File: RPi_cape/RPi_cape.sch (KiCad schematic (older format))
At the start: 109 parts, among them J1 Conn_01x04, J10 Conn_01x02, J11 Conn_01x02, J12 Conn_01x02, J16 Conn_01x06, J2 Conn_01x02, J3 Conn_01x02, J4 Conn_01x02, J5 Conn_01x03, J6 Conn_01x03, J7 Conn_01x02, J8 Conn_02x20_Odd_Even, J9 Conn_01x02, U1 TL431A, U2 ADC128D818, U3 ADC128D818

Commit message: Better valve monitoring, finalized layout and manufacturing files
Created assembly and fabrication drawings, assigned all BOM parts, generally made design ready for ordering
Added strain-relief slots and barb mounting dimensions for digital pressure sensors
Changed valve drivers from discrete power MOSFETs to "smart" industrial/automotive driver ICs for the current monitoring, including valve-movement monitor for #4
Connected RPi_Valve* signals to larger CPLD footprint, changed Raspberry Pi pin assignment as a result to ease PCB routing
Updated footprints, page layout to create readable assembly drawing
Added current-measurement testpoints for CPLD power from BATT+
Changed power diodes in power-down-alarm circuit to small-signal parts for more compact layout
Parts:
- removed C15, C16, C17, C18: 100uF 50V AlPoly, Capacitor_SMD:CP_Elec_10x10.5, symbol Device:CP1
- removed H5: #4/M3, MountingHole:MountingHole_3.2mm_M3_Pad_Via, symbol Mechanical:MountingHole_Pad
- added C29, C30, C49: 10nF 50V NP0, Capacitor_SMD:C_0603_1608Metric, symbol Device:C
- D1, D2: footprint Diode_SMD:D_SMA -> Ventilator:D_SMA
- D3: footprint Diode_SMD:D_SOD-123 -> Ventilator:D_SOD-123; Manufacturer (none) -> ON Semiconductor; Part Number (none) -> MMSZ5231BT1G
- D4, D5, D6, D7, D8, D9: footprint LED_SMD:LED_0805_2012Metric -> Ventilator:LED_0805_2012Metric
- R1, R2: Manufacturer (none) -> KOA Speer; Part Number (none) -> RK73H2BTTD1001F
- R10, R16, R18: Manufacturer (none) -> KOA Speer; Part Number (none) -> RK73H2BTTD10R0F
- R11, R4: Manufacturer (none) -> Panasonic; Part Number (none) -> ERJ-8GEY0R00V
- R12, R13, R19, R192, R195, R196, R197, R25, R26, R27, R28, R6, R7: Manufacturer (none) -> KOA Speer; Part Number (none) -> RK73H2BTTD1002F
- R14, R15, R17, R193, R194: Manufacturer (none) -> KOA Speer; Part Number (none) -> RK73H2BTTD3301F
- R20, R22: Manufacturer (none) -> KOA Speer; Part Number (none) -> RK73H2BTTD2202F
- R29: Manufacturer (none) -> KOA Speer; Part Number (none) -> RK73H2BTTD1501F
- R5: Manufacturer (none) -> Panasonic; Part Number (none) -> ERJ-8RQF1R0V
- R8: value 10K -> DNP
- R9: value 1K -> DNP
- U1: footprint Package_TO_SOT_SMD:SOT-23 -> Ventilator:SOT-23
- U2, U3: footprint Package_SO:TSSOP-16_4.4x5mm_P0.65mm -> Ventilator:TSSOP-16_4.4x5mm_P0.65mm
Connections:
- net CPLD_ADC3: now also C29.2
- net CPLD_ADC4: now also C30.2
- net CPLD_ADC5: now also C49.2
- net CPLD_ADC6: now also C5.2, R8.2, R9.1; no longer C4.2, R6.2, R7.1
- net CPLD_ADC7: now also C4.2, R6.2, R7.1; no longer C5.2, R8.2, R9.1
- net GND: now also C29.1, C30.1, C49.1
- net Output Driver 1/OutH: now also J9.2 (Pin_2); no longer J9.1 (Pin_1)
- net Output Driver 1/OutL: now also J9.1 (Pin_1); no longer J9.2 (Pin_2)
- net Output Driver 2/OutH: now also J10.2 (Pin_2); no longer J10.1 (Pin_1)
- net Output Driver 2/OutL: now also J10.1 (Pin_1); no longer J10.2 (Pin_2)
- net Output Driver 3/OutH: now also J11.2 (Pin_2); no longer J11.1 (Pin_1)
- net Output Driver 3/OutL: now also J11.1 (Pin_1); no longer J11.2 (Pin_2)
- net Output Driver 4/OutH: now also J12.2 (Pin_2); no longer J12.1 (Pin_1)
- net Output Driver 4/OutL: now also J12.1 (Pin_1); no longer J12.2 (Pin_2)
- net RPi_Alarm_Spkr: now also J8.11 (Pin_11); no longer J8.21 (Pin_21)
- net RPi_valve1: now also J8.40 (Pin_40); no longer J8.11 (Pin_11)
- net RPi_valve2: now also J8.38 (Pin_38); no longer J8.13 (Pin_13)
- net RPi_valve3: now also J8.36 (Pin_36); no longer J8.15 (Pin_15)
- net RPi_valve4: now also J8.32 (Pin_32); no longer J8.19 (Pin_19)
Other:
- note added: "Alarm(s)"
- note added: "Populate (10K, 1K) if not using\nthe valve driver current sense"
- note added: "When analog current sense drivers used,\nCPLD fault input for valve 4 is handled by\n"valve motion detection" circuit\n(all other valve fault inputs are inactive)"
- moved on the sheet: F4, F5, J10, J11, J12, J5, J6, J7, J9

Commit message: Manufacturing clean-up
Corrections and additions to BOM etc. for manufacturing
Added power draw tracking spreadsheet
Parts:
- C113, C40, C43: Manufacturer Murata -> AVX; Part Number GRM1885C1H103JA01D -> 06035A102JAT2A
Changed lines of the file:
@@
 F 2 "Capacitor_SMD:C_0603_1608Metric" H 11338 9700 50  0001 C CNN
 F 3 "~" H 11300 9850 50  0001 C CNN
-F 4 "Murata" H 11300 9850 50  0001 C CNN "Manufacturer"
-F 5 "GRM1885C1H103JA01D" H 11300 9850 50  0001 C CNN "Part Number"
+F 4 "AVX" H 11300 9850 50  0001 C CNN "Manufacturer"
+F 5 "06035A102JAT2A" H 11300 9850 50  0001 C CNN "Part Number"
 	1    11300 9850
 	-1   0    0    1
@@
 F 2 "Capacitor_SMD:C_0603_1608Metric" H 11588 9700 50  0001 C CNN
 F 3 "~" H 11550 9850 50  0001 C CNN
-F 4 "Murata" H 11550 9850 50  0001 C CNN "Manufacturer"
-F 5 "GRM1885C1H103JA01D" H 11550 9850 50  0001 C CNN "Part Number"
+F 4 "AVX" H 11550 9850 50  0001 C CNN "Manufacturer"
+F 5 "06035A102JAT2A" H 11550 9850 50  0001 C CNN "Part Number"
 	1    11550 9850
 	-1   0    0    1
@@
 F 2 "Capacitor_SMD:C_0603_1608Metric" H 10488 10000 50  0001 C CNN
 F 3 "~" H 10450 10150 50  0001 C CNN
-F 4 "Murata" H 10450 10150 50  0001 C CNN "Manufacturer"
-F 5 "GRM1885C1H103JA01D" H 10450 10150 50  0001 C CNN "Part Number"
+F 4 "AVX" H 10450 10150 50  0001 C CNN "Manufacturer"
+F 5 "06035A102JAT2A" H 10450 10150 50  0001 C CNN "Part Number"
 	1    10450 10150
 	-1   0    0    1

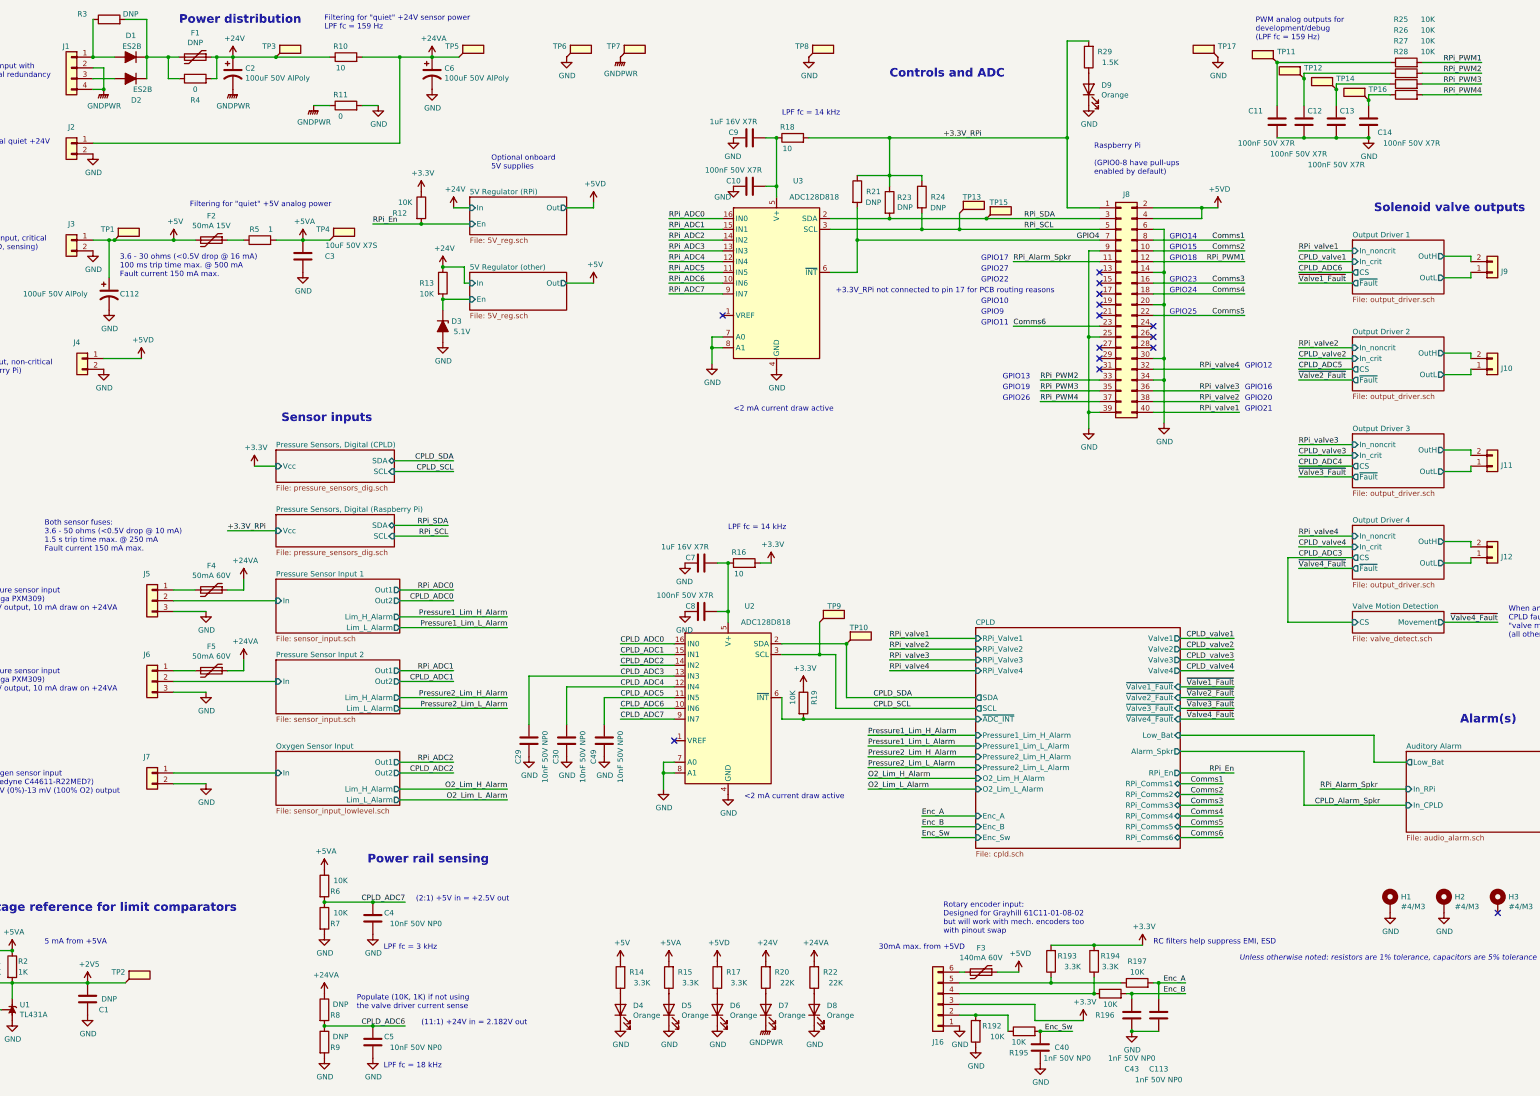
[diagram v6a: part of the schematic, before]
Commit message: Safety additions
Switched CPLD_ADC7 to +24V monitoring (from +5V monitoring), and added CPLD ~Bat_On digital input(s) to know when it's running from backup battery, to cover low-input-voltage edge cases
Added series 1K resistors (R226-231) on CPLD<->RPi Comms1-6 lines, to protect CPLD in case of overvoltage from RPi failure
Added optional input TVS D23 to handle sustained over-voltage or large surges
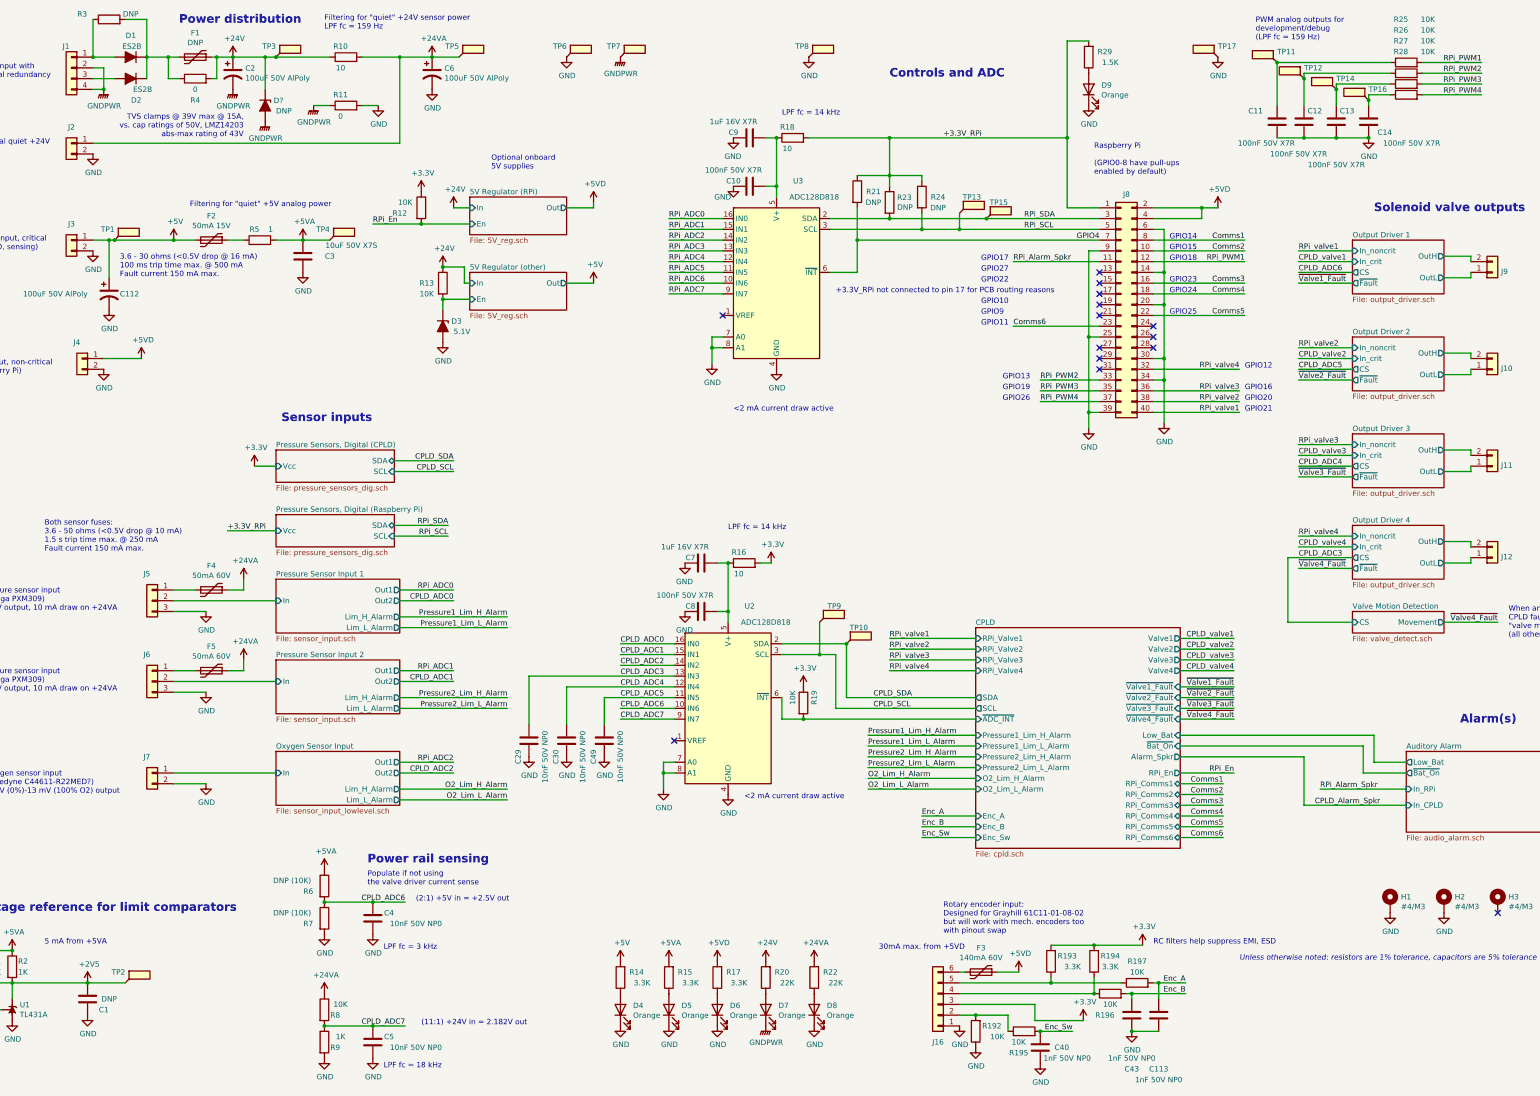
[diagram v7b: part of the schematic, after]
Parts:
- added D?: DNP, Ventilator:D_SMB, symbol Device:D_Zener_ALT
- R6, R7: value 10K -> DNP (10K)
- R8: value DNP -> 10K; Manufacturer (none) -> KOA Speer; Part Number (none) -> RK73H2BTTD1002F
- R9: value DNP -> 1K; Manufacturer (none) -> KOA Speer; Part Number (none) -> RK73H2BTTD1001F
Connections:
- net +24V: now also D?.1 (K)
- net CPLD_ADC6: now also C4.2, R6.2, R7.1; no longer C5.2, R8.2, R9.1
- net CPLD_ADC7: now also C5.2, R8.2, R9.1; no longer C4.2, R6.2, R7.1
- net GNDPWR: now also D?.2 (A)
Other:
- note added: "Populate if not using\nthe valve driver current sense"
- note added: "TVS clamps @ 39V max @ 15A,\nvs. cap ratings of 50V, LMZ14203\nabs-max rating of 43V"
- note removed: "Populate (10K, 1K) if not using\nthe valve driver current sense"
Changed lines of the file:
@@
 Title "Raspberry Pi Hat for JamVent Adaptation"
 Date ""
-Rev "1.5"
+Rev "1.6"
 Comp "Partners COVID Innovation Group"
 Comment1 "Don Straney"
@@
 F3 "In_CPLD" I L 13850 7900 50
 F4 "Low_Bat" O L 13850 7500 50
+F5 "~Bat_On" O L 13850 7600 50
 $EndSheet
 $Comp
@@
 $EndComp
 Wire Wire Line
-	2950 950  3350 950
+	2950 950  3250 950
 $Comp
 L Ventilator:+24VA #PWR029
@@
 AR Path="/5E9D7F90" Ref="R6"  Part="1"
 AR Path="/5E8AFE9D/5E9D7F90" Ref="R?"  Part="1"
-F 0 "R6" H 3900 8600 50  0000 C CNN
-F 1 "10K" H 3950 8700 50  0000 C CNN
+F 0 "R6" H 3650 8600 50  0000 C CNN
+F 1 "DNP (10K)" H 3500 8700 50  0000 C CNN
 F 2 "Resistor_SMD:R_1206_3216Metric" V 3730 8650 50  0001 C CNN
 F 3 "~" H 3800 8650 50  0001 C CNN
@@
 AR Path="/5E9DF1E8" Ref="R7"  Part="1"
 AR Path="/5E8AFE9D/5E9DF1E8" Ref="R?"  Part="1"
-F 0 "R7" H 3900 8900 50  0000 C CNN
-F 1 "10K" H 3950 9000 50  0000 C CNN
+F 0 "R7" H 3650 8900 50  0000 C CNN
+F 1 "DNP (10K)" H 3500 9000 50  0000 C CNN
 F 2 "Resistor_SMD:R_1206_3216Metric" V 3730 8950 50  0001 C CNN
 F 3 "~" H 3800 8950 50  0001 C CNN
@@
 AR Path="/5E8AFE9D/5E9DF420" Ref="R?"  Part="1"
 F 0 "R8" H 3900 9750 50  0000 C CNN
-F 1 "DNP" H 3950 9850 50  0000 C CNN
+F 1 "10K" H 3950 9850 50  0000 C CNN
 F 2 "Resistor_SMD:R_1206_3216Metric" V 3730 9800 50  0001 C CNN
 F 3 "~" H 3800 9800 50  0001 C CNN
+F 4 "KOA Speer" H 3800 9800 50  0001 C CNN "Manufacturer"
+F 5 "RK73H2BTTD1002F" H 3800 9800 50  0001 C CNN "Part Number"
 	1    3800 9800
 	1    0    0    -1
@@
 AR Path="/5E8AFE9D/5E9DF8CA" Ref="R?"  Part="1"
 F 0 "R9" H 3900 10050 50  0000 C CNN
-F 1 "DNP" H 3950 10150 50  0000 C CNN
+F 1 "1K" H 3950 10150 50  0000 C CNN
 F 2 "Resistor_SMD:R_1206_3216Metric" V 3730 10100 50  0001 C CNN
 F 3 "~" H 3800 10100 50  0001 C CNN
+F 4 "KOA Speer" H 3800 10100 50  0001 C CNN "Manufacturer"
+F 5 "RK73H2BTTD1001F" H 3800 10100 50  0001 C CNN "Part Number"
 	1    3800 10100
 	1    0    0    -1
@@
 Wire Wire Line
 	4500 7850 5500 7850
-$Sheet
-S 9850 6250 1900 2050
-U 5E8C8865
-F0 "CPLD" 50
-F1 "cpld.sch" 50
-F2 "Valve1" O R 11750 6350 50
-F3 "Valve2" O R 11750 6450 50
-F4 "Valve3" O R 11750 6550 50
-F5 "Valve4" O R 11750 6650 50
-F6 "RPi_Valve1" I L 9850 6350 50
-F7 "RPi_Valve2" I L 9850 6450 50
-F8 "RPi_Valve3" I L 9850 6550 50
-F9 "RPi_Valve4" I L 9850 6650 50
-F10 "Pressure1_Lim_H_Alarm" I L 9850 7250 50
-F11 "Pressure1_Lim_L_Alarm" I L 9850 7350 50
-F12 "Pressure2_Lim_H_Alarm" I L 9850 7450 50
-F13 "Pressure2_Lim_L_Alarm" I L 9850 7550 50
-F14 "O2_Lim_H_Alarm" I L 9850 7650 50
-F15 "O2_Lim_L_Alarm" I L 9850 7750 50
-F16 "Alarm_Spkr" O R 11750 7400 50
-F17 "SDA" O L 9850 6900 50
-F18 "SCL" O L 9850 7000 50
-F19 "~ADC_INT" I L 9850 7100 50
-F20 "Low_Bat" I R 11750 7250 50
-F21 "RPi_Comms1" B R 11750 7700 50
-F22 "RPi_Comms2" B R 11750 7800 50
-F23 "RPi_Comms3" B R 11750 7900 50
-F24 "RPi_Comms4" B R 11750 8000 50
-F25 "RPi_Comms5" B R 11750 8100 50
-F26 "RPi_Comms6" B R 11750 8200 50
-F27 "RPi_En" O R 11750 7600 50
-F28 "Enc_A" I L 9850 8000 50
-F29 "Enc_B" I L 9850 8100 50
-F30 "Enc_Sw" I L 9850 8200 50
-F31 "~Valve1_Fault" I R 11750 6800 50
-F32 "~Valve2_Fault" I R 11750 6900 50
-F33 "~Valve4_Fault" I R 11750 7100 50
-F34 "~Valve3_Fault" I R 11750 7000 50
-$EndSheet
 Wire Wire Line
 	9850 6350 9050 6350
@@
 Text Label 6550 7100 0    50   ~ 0
 CPLD_ADC7
-Text Label 4550 9950 2    50   ~ 0
-CPLD_ADC6
 Text Label 4550 8800 2    50   ~ 0
+CPLD_ADC6
+Text Label 4550 9950 2    50   ~ 0
 CPLD_ADC7
 Wire Wire Line
@@
 GPIO9
 Wire Wire Line
-	12900 7400 12900 7900
+	12900 7450 12900 7900
 Wire Wire Line
 	12900 7900 13850 7900
@@
 	11750 7250 13550 7250
 Wire Wire Line
-	11750 7400 12900 7400
+	11750 7450 12900 7450
 Wire Wire Line
 	11750 7700 12150 7700
@@
 Text Label 12850 2950 0    50   ~ 0
 CPLD_ADC6
-Text Notes 4100 9800 0    50   ~ 0
-Populate (10K, 1K) if not using\nthe valve driver current sense
+Text Notes 4200 8650 0    50   ~ 0
+Populate if not using\nthe valve driver current sense
 $Comp
 L Connector_Generic:Conn_02x20_Odd_Even J8
@@
 Text Notes 14350 7150 0    79   ~ 16
 Alarm(s)
+Wire Wire Line
+	13850 7600 13450 7600
+Wire Wire Line
+	13450 7600 13450 7350
+Wire Wire Line
+	13450 7350 11750 7350
+$Sheet
+S 9850 6250 1900 2050
+U 5E8C8865
+F0 "CPLD" 50
+F1 "cpld.sch" 50
+F2 "Valve1" O R 11750 6350 50
+F3 "Valve2" O R 11750 6450 50
+F4 "Valve3" O R 11750 6550 50
+F5 "Valve4" O R 11750 6650 50
+F6 "RPi_Valve1" I L 9850 6350 50
+F7 "RPi_Valve2" I L 9850 6450 50
+F8 "RPi_Valve3" I L 9850 6550 50
+F9 "RPi_Valve4" I L 9850 6650 50
+F10 "Pressure1_Lim_H_Alarm" I L 9850 7250 50
+F11 "Pressure1_Lim_L_Alarm" I L 9850 7350 50
+F12 "Pressure2_Lim_H_Alarm" I L 9850 7450 50
+F13 "Pressure2_Lim_L_Alarm" I L 9850 7550 50
+F14 "O2_Lim_H_Alarm" I L 9850 7650 50
+F15 "O2_Lim_L_Alarm" I L 9850 7750 50
+F16 "Alarm_Spkr" O R 11750 7450 50
+F17 "SDA" O L 9850 6900 50
+F18 "SCL" O L 9850 7000 50
+F19 "~ADC_INT" I L 9850 7100 50
+F20 "Low_Bat" I R 11750 7250 50
+F21 "RPi_Comms1" B R 11750 7700 50
+F22 "RPi_Comms2" B R 11750 7800 50
+F23 "RPi_Comms3" B R 11750 7900 50
+F24 "RPi_Comms4" B R 11750 8000 50
+F25 "RPi_Comms5" B R 11750 8100 50
+F26 "RPi_Comms6" B R 11750 8200 50
+F27 "RPi_En" O R 11750 7600 50
+F28 "Enc_A" I L 9850 8000 50
+F29 "Enc_B" I L 9850 8100 50
+F30 "Enc_Sw" I L 9850 8200 50
+F31 "~Valve1_Fault" I R 11750 6800 50
+F32 "~Valve2_Fault" I R 11750 6900 50
+F33 "~Valve4_Fault" I R 11750 7100 50
+F34 "~Valve3_Fault" I R 11750 7000 50
+F35 "~Bat_On" I R 11750 7350 50
+$EndSheet
+$Comp
+L Device:D_Zener_ALT D?
+U 1 1 5F21EF66
+P 3250 1400
+AR Path="/5F21EF66" Ref="D?"  Part="1"
+AR Path="/5E8AFE9D/5F21EF66" Ref="D?"  Part="1"
+AR Path="/5E8FBD97/5F21EF66" Ref="D?"  Part="1"
+AR Path="/5E8DEDC0/5F21EF66" Ref="D?"  Part="1"
+AR Path="/5E8DFCAD/5F21EF66" Ref="D?"  Part="1"
+AR Path="/5E8E0754/5F21EF66" Ref="D?"  Part="1"
+F 0 "D?" V 3204 1479 50  0000 L CNN
+F 1 "DNP" V 3300 1500 50  0000 L CNN
+F 2 "Ventilator:D_SMB" H 3250 1400 50  0001 C CNN
+F 3 "~" H 3250 1400 50  0001 C CNN
+F 4 "Littelfuse" H 3250 1400 50  0001 C CNN "Manufacturer"
+F 5 "SMBJ24A" H 3250 1400 50  0001 C CNN "Part Number"
+	1    3250 1400
+	0    1    1    0
+$EndComp
+$Comp
+L power:GNDPWR #PWR?
+U 1 1 5F23EB06
+P 3250 1550
+AR Path="/5E8FBD97/5F23EB06" Ref="#PWR?"  Part="1"
+AR Path="/5E8DEDC0/5F23EB06" Ref="#PWR?"  Part="1"
+AR Path="/5E8DFCAD/5F23EB06" Ref="#PWR?"  Part="1"
+AR Path="/5E8E0754/5F23EB06" Ref="#PWR?"  Part="1"
+AR Path="/5F23EB06" Ref="#PWR?"  Part="1"
+F 0 "#PWR?" H 3250 1350 50  0001 C CNN
+F 1 "GNDPWR" H 3254 1396 50  0000 C CNN
+F 2 "" H 3250 1500 50  0001 C CNN
+F 3 "" H 3250 1500 50  0001 C CNN
+	1    3250 1550
+	1    0    0    -1
+$EndComp
+Wire Wire Line
+	3250 1250 3250 950
+Connection ~ 3250 950
+Wire Wire Line
+	3250 950  3350 950
+Text Notes 3050 1700 2    50   ~ 0
+TVS clamps @ 39V max @ 15A,\nvs. cap ratings of 50V, LMZ14203\nabs-max rating of 43V
 $EndSCHEMATC

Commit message: Cleanup, docs
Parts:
- gave numbers to parts that had none: 1
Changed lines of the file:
@@
 $EndSheet
 $Comp
-L Device:D_Zener_ALT D?
+L Device:D_Zener_ALT D23
 U 1 1 5F21EF66
 P 3250 1400
-AR Path="/5F21EF66" Ref="D?"  Part="1"
+AR Path="/5F21EF66" Ref="D23"  Part="1"
 AR Path="/5E8AFE9D/5F21EF66" Ref="D?"  Part="1"
 AR Path="/5E8FBD97/5F21EF66" Ref="D?"  Part="1"
@@
 AR Path="/5E8DFCAD/5F21EF66" Ref="D?"  Part="1"
 AR Path="/5E8E0754/5F21EF66" Ref="D?"  Part="1"
-F 0 "D?" V 3204 1479 50  0000 L CNN
+F 0 "D23" V 3204 1479 50  0000 L CNN
 F 1 "DNP" V 3300 1500 50  0000 L CNN
 F 2 "Ventilator:D_SMB" H 3250 1400 50  0001 C CNN
@@
 AR Path="/5E8DFCAD/5F23EB06" Ref="#PWR?"  Part="1"
 AR Path="/5E8E0754/5F23EB06" Ref="#PWR?"  Part="1"
-AR Path="/5F23EB06" Ref="#PWR?"  Part="1"
-F 0 "#PWR?" H 3250 1350 50  0001 C CNN
+AR Path="/5F23EB06" Ref="#PWR0374"  Part="1"
+F 0 "#PWR0374" H 3250 1350 50  0001 C CNN
 F 1 "GNDPWR" H 3254 1396 50  0000 C CNN
 F 2 "" H 3250 1500 50  0001 C CNN
